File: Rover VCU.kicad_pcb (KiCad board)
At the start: 4 copper layers, 86.2 x 39 mm, 101 parts, among them J1 Conn_ST_STDC14, J2 USB4105-GF-A, J3 430450400, J6 430451200, SW1 TS-1088-AR02016, U1 STM32H563RITx, U3 DP83TC812RRHARQ1, U4 SN65HVD230, U5 SN65HVD230, U6 LMR51610, U7 NXE2S0505MC, U8 NCP1117-3.3_SOT223, Y1 32.768kHz

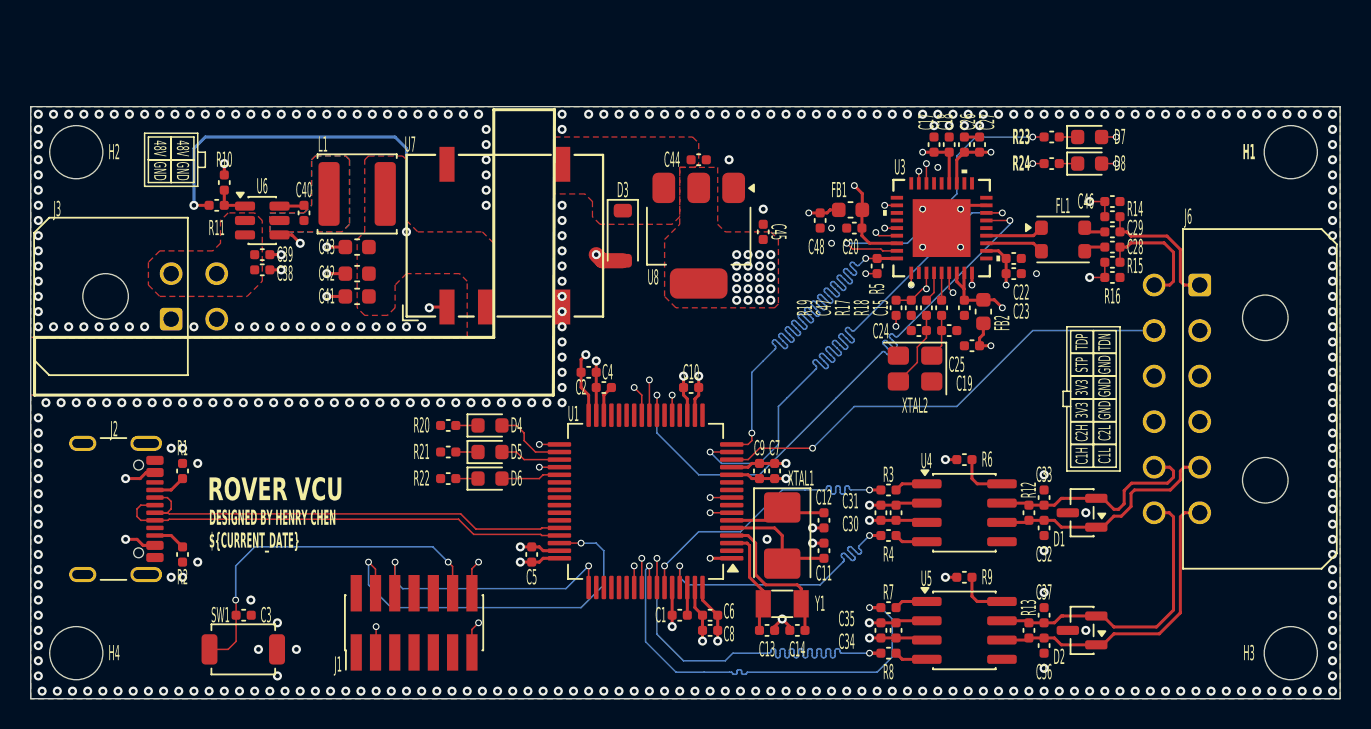
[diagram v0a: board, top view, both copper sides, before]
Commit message: feat: implmeneted revamp with normal ethernet LAN8742A
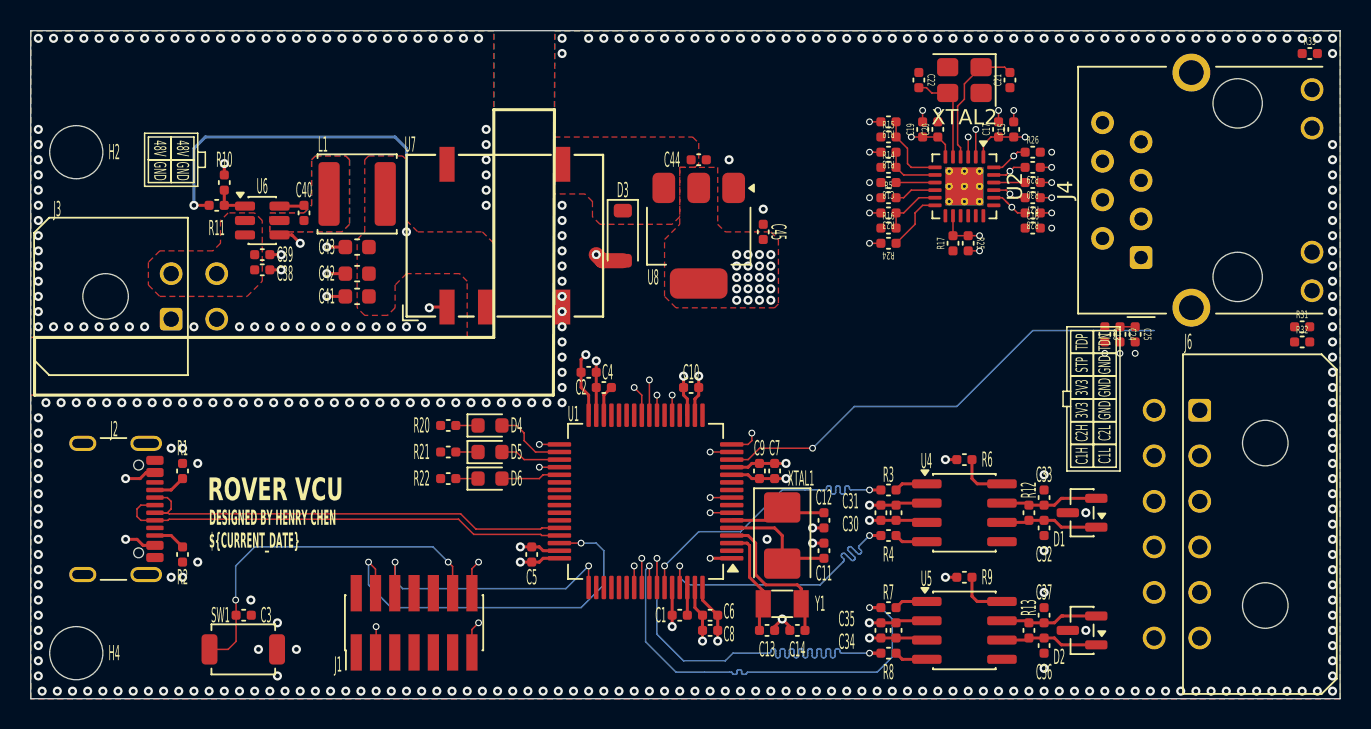
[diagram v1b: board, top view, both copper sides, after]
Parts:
- removed C26, C28, C29: 100nF, chenry-footprint-lib:C_0402
- removed C27: 2.2uF, chenry-footprint-lib:C_0402
- removed C46: 4.7uF, chenry-footprint-lib:C_0402
- removed C47, C48: 1uF, chenry-footprint-lib:C_0402
- removed D7, D8: LED_RED_0603, LED_SMD:LED_0603_1608Metric
- removed FB1, FB2: 600Ohm @ 100MHz, Capacitor_SMD:C_0603_1608Metric
- removed FL1: 9kOhm@10MHz & 10kOhm@100Mhz, Inductor_SMD:L_CommonModeChoke_Coilank_ACM3225
- removed H1, H3: MountingHole, MountingHole:MountingHole_3.5mm
- removed U3: DP83TC812RRHARQ1, chenry-footprint-lib:VQFN36_RHA_TEX
- added C16: 100nF, chenry-footprint-lib:C_0402, F.Cu at (168.8, 88.0)
- added C21: 20pF, chenry-footprint-lib:C_0402, F.Cu at (167.2, 78.2)
- added J4: RJ45_Hanrun_HR911105A_Horizontal, chenry-footprint-lib:RJ45_Hanrun_HR911105A_Horizontal, F.Cu at (175.9, 89.9)
- added R25: 10K, chenry-footprint-lib:R_0402, F.Cu at (164.5, 89.0)
- added R26: 12.1K, chenry-footprint-lib:R_0402, F.Cu at (168.8, 83.0)
- added R27: 49.9R, chenry-footprint-lib:R_0402, F.Cu at (168.8, 86.0)
- added R28: 49.9R, chenry-footprint-lib:R_0402, F.Cu at (168.8, 87.0)
- added R29: 49.9R, chenry-footprint-lib:R_0402, F.Cu at (168.8, 84.0)
- added R30: 49.9R, chenry-footprint-lib:R_0402, F.Cu at (168.8, 85.0)
- added R31: 10K, chenry-footprint-lib:R_0402, F.Cu at (186.5, 94.5)
- added R32: 330R, chenry-footprint-lib:R_0402, F.Cu at (186.5, 95.5)
- added R33: 330R, chenry-footprint-lib:R_0402, F.Cu at (187.0, 76.5)
- added U2: LAN8742A, chenry-footprint-lib:VQFN-24-1EP_4x4mm_P0.5mm_EP2.5x2.5mm_ThermalVias, F.Cu at (164.2, 85.2)
- C15: value 100nF -> 10uF
- C17, C23: value 10nF -> 100nF
- C18: value 470nF -> 100nF
- C20: value 10nF -> 100pF
- C22: value 470nF -> 20pF
- C24, C25: value 22pF -> 100nF
- R14, R15: value 1K -> 33R
- R16: value 100K -> 33R
- R17: value 100R -> 33R
- R18: value 100R -> 10K
- R19, R5: value 2K2 -> 10K
- R23, R24: value 5K1 -> 10K
- moved XTAL2 19.3 mm to (164.2, 78.2)
- moved R15 16.9 mm to (159.2, 82.0), turned to 0 degrees
- moved R14 15.1 mm to (159.2, 84.0), turned to 0 degrees
- moved R16 15.1 mm to (159.2, 88.0)
- moved C19 14.6 mm to (161.5, 81.5), turned to 90 degrees
- moved C22 13.3 mm to (161.2, 78.2), turned to -90 degrees
- moved C24 13.3 mm to (174.5, 95.0), turned to -90 degrees
- moved R19 12.3 mm to (159.2, 81.0), turned to 180 degrees
- moved C25 12.3 mm to (175.5, 95.0), turned to -90 degrees
- moved C15 12.2 mm to (167.5, 81.5), turned to 90 degrees
- moved R24 12.0 mm to (159.2, 89.0)
- moved R23 11.9 mm to (159.2, 87.0)
- moved R18 10.8 mm to (159.2, 83.0), turned to 180 degrees
- moved C20 8.51 mm to (162.5, 81.5), turned to 90 degrees
- moved J6 8.25 mm to (179.8, 100.0)
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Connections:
- C15 pad 1: Net-(U3-VDDA) -> Net-(U2-VDD1A)
- C17 pad 1: Net-(U3-VDDIO) -> Net-(U2-VDD1A)
- C18 pad 1: Net-(U3-VDDIO) -> Net-(U2-VDDIO)
- C19 pad 1: /VDD_3V3 -> Net-(U2-VDDCR)
- C20 pad 1: Net-(U3-VDDIO) -> Net-(U2-VDDCR)
- C22 pad 1: Net-(U3-VDDA) -> GND
- C22 pad 2: GND -> Net-(U2-XTAL1/CLKIN)
- C23 pad 1: Net-(U3-VDDA) -> /VDD_3V3
- C24 pad 1: Net-(C24-Pad1) -> /VDD_3V3
- C25 pad 1: Net-(C25-Pad1) -> /VDD_3V3
- J6 pad 1: /TRD_N -> unconnected-(J6-Pin_1-Pad1)
- J6 pad 7: /TRD_P -> unconnected-(J6-Pin_7-Pad7)
- R14 pad 1: /TRD_N -> /MCU/RMII_RXD0
- R14 pad 2: Net-(C46-Pad1) -> Net-(U2-RXD0/MODE0)
- R15 pad 1: /TRD_P -> /MCU/RMII_RXD1
- R15 pad 2: Net-(C46-Pad1) -> Net-(U2-RXD1/MODE1)
- R16 pad 1: Net-(C46-Pad1) -> /MCU/RMII_CRS_DV
- R16 pad 2: GND -> Net-(U2-CRS_DV/MODE2)
- R17 pad 1: Net-(U3-XO) -> /MCU/RMII_REF_CLK
- R17 pad 2: Net-(C24-Pad1) -> Net-(U2-~{INT}/REFCLKO)
- R18 pad 1: Net-(U3-XI) -> Net-(U2-RXD0/MODE0)
- R18 pad 2: Net-(C25-Pad1) -> /VDD_3V3
- R19 pad 1: /VDD_3V3 -> Net-(U2-RXD1/MODE1)
- R19 pad 2: /MCU/NRST -> /VDD_3V3
- R23 pad 1: Net-(D7-K) -> Net-(U2-CRS_DV/MODE2)
- R23 pad 2: Net-(U3-LED_0) -> /VDD_3V3
- R24 pad 1: Net-(D8-K) -> /MCU/RMII_MDIO
- R24 pad 2: Net-(U3-LED_1) -> /VDD_3V3
- R5 pad 1: /VDD_3V3 -> GND
- R5 pad 2: /MCU/RMII_MDIO -> Net-(U2-RXER/PHYAD0)
- XTAL2 pad 1: Net-(C25-Pad1) -> Net-(U2-XTAL2)
- XTAL2 pad 3: Net-(C24-Pad1) -> Net-(U2-XTAL1/CLKIN)
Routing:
- net /MCU/RMII_MDC: track 43.5 -> 1.43 mm, vias 2 -> 1
- net /MCU/RMII_TXD1: track 42.6 -> 1.32 mm, vias 2 -> 1
- net /MCU/RMII_TXD0: track 42.5 -> 1.33 mm, vias 2 -> 1
- net /MCU/RMII_TX_EN: track 42.5 -> 1.33 mm, vias 2 -> 1
- net /MCU/RMII_RXD1: track 42.6 -> 2.03 mm, vias 2 -> 1
- net /MCU/RMII_RXD0: track 42.5 -> 2.33 mm, vias 2 -> 1
- net /MCU/RMII_CRS_DV: track 39.8 -> 1.33 mm, vias 2 -> 1
- net /MCU/RMII_REF_CLK: track 39.7 -> 1.43 mm, vias 2 -> 1
- net /MCU/RMII_MDIO: track 39.4 -> 5.97 mm, vias 2 -> 1
- net /MCU/NRST: track 80.6 -> 52.8 mm, vias 4 -> 3
- net Net-(U3-LED_0): track 20.9 -> 0.00 mm, vias 2 -> 0
- net Net-(U3-VDDIO): track 16.1 -> 0.00 mm, vias 2 -> 0
- net Net-(U3-LED_1): track 15.4 -> 0.00 mm, vias 2 -> 0
- net /CAN2_N: track 20.6 -> 6.45 mm
- net Net-(U3-PIN_21): track 14.1 -> 0.00 mm, vias 2 -> 0
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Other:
- board size 86.2 x 39 mm -> 86.2 x 44 mm
